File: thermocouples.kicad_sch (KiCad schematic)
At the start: 21 parts, among them J1 Conn_02x15_Odd_Even, J2 Conn_02x15_Odd_Even, J3 Conn_01x02, J4 Conn_01x02, U1 ADS1120-RVA

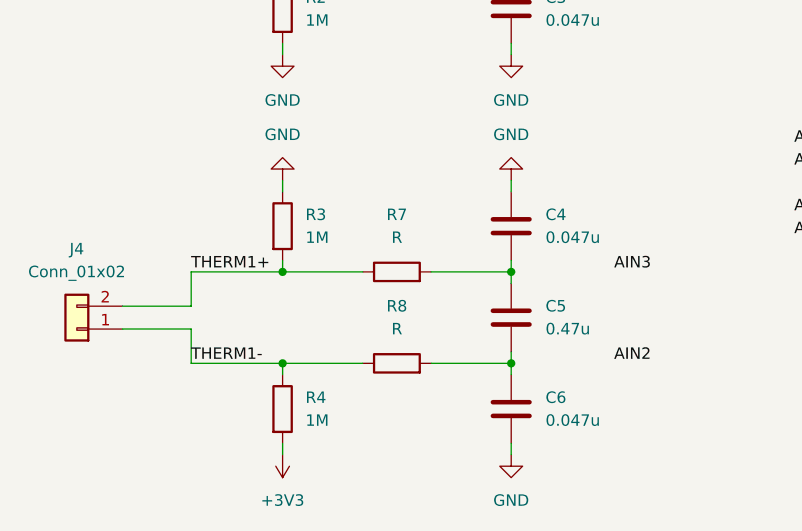
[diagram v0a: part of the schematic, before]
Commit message: sourced all components on lcsc, added ibom and outputs
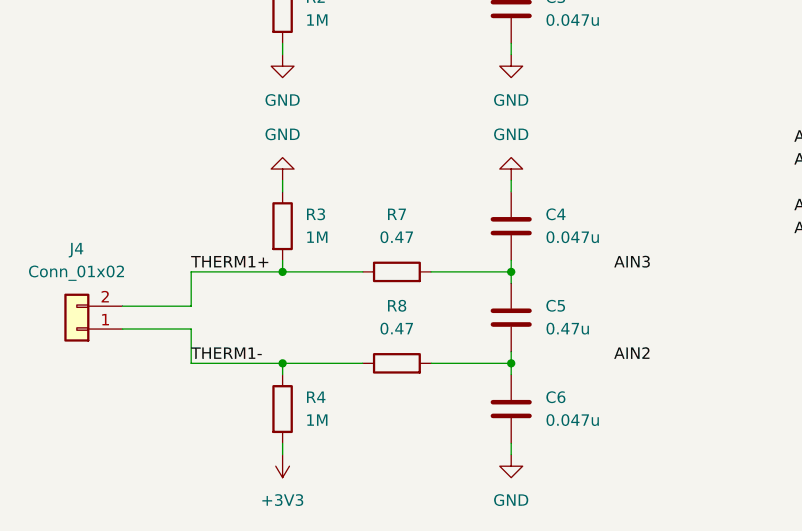
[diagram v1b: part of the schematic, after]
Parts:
- C1, C3, C4, C6: LCSC (none) -> C1622
- C2, C5: LCSC (none) -> C1623
- C7, C8: LCSC (none) -> C1591
- J1, J2, J3, J4: LCSC (none) -> C429959
- R1, R2, R3, R4: LCSC (none) -> C26098
- R5, R6: LCSC (none) -> C23411
- R7, R8: value R -> 0.47; LCSC (none) -> C23411
- U1: LCSC (none) -> C2861236
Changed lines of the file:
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@@
+      (effects (font (size 1.27 1.27)) hide)
+    )
+    (property "LCSC" "C1622" (id 4) (at 69.85 93.98 0)
       (effects (font (size 1.27 1.27)) hide)
     )
@@
     )
     (property "Datasheet" "~" (id 3) (at 247.65 107.315 0)
+      (effects (font (size 1.27 1.27)) hide)
+    )
+    (property "LCSC" "C429959" (id 4) (at 247.65 107.315 0)
       (effects (font (size 1.27 1.27)) hide)
     )
@@
       (effects (font (size 1.27 1.27)) hide)
     )
+    (property "LCSC" "C2861236" (id 4) (at 123.19 114.3 0)
+      (effects (font (size 1.27 1.27)) hide)
+    )
     (pin "1")
     (pin "10")
@@
       (effects (font (size 1.27 1.27)) hide)
     )
+    (property "LCSC" "C26098" (id 4) (at 44.45 73.66 0)
+      (effects (font (size 1.27 1.27)) hide)
+    )
     (pin "1")
     (pin "2")
@@
     )
     (property "Datasheet" "~" (id 3) (at 69.85 128.27 0)
+      (effects (font (size 1.27 1.27)) hide)
+    )
+    (property "LCSC" "C1623" (id 4) (at 69.85 128.27 0)
       (effects (font (size 1.27 1.27)) hide)
     )
@@
     )
     (property "Datasheet" "~" (id 3) (at 247.65 55.88 0)
+      (effects (font (size 1.27 1.27)) hide)
+    )
+    (property "LCSC" "C429959" (id 4) (at 247.65 55.88 0)
       (effects (font (size 1.27 1.27)) hide)
     )
@@
     (in_bom yes) (on_board yes) (fields_autoplaced)
     (property "Reference" "R8" (id 0) (at 57.15 127 90))
-    (property "Value" "R" (id 1) (at 57.15 129.54 90))
+    (property "Value" "0.47" (id 1) (at 57.15 129.54 90))
     (property "Footprint" "Resistor_SMD:R_0603_1608Metric_Pad0.98x0.95mm_HandSolder" (id 2) (at 57.15 135.128 90)
       (effects (font (size 1.27 1.27)) hide)
     )
     (property "Datasheet" "~" (id 3) (at 57.15 133.35 0)
+      (effects (font (size 1.27 1.27)) hide)
+    )
+    (property "LCSC" "C23411" (id 4) (at 57.15 133.35 0)
       (effects (font (size 1.27 1.27)) hide)
     )
@@
       (effects (font (size 1.27 1.27)) hide)
     )
+    (property "LCSC" "C429959" (id 4) (at 21.59 85.09 0)
+      (effects (font (size 1.27 1.27)) hide)
+    )
     (pin "1")
     (pin "2")
@@
       (effects (font (size 1.27 1.27)) hide)
     )
+    (property "LCSC" "C1622" (id 4) (at 69.85 73.66 0)
+      (effects (font (size 1.27 1.27)) hide)
+    )
     (pin "1")
     (pin "2")
@@
     )
     (property "Datasheet" "~" (id 3) (at 132.08 92.71 0)
+      (effects (font (size 1.27 1.27)) hide)
+    )
+    (property "LCSC" "C1591" (id 4) (at 132.08 92.71 0)
       (effects (font (size 1.27 1.27)) hide)
     )
@@
       (effects (font (size 1.27 1.27)) hide)
     )
+    (property "LCSC" "C429959" (id 4) (at 21.59 129.54 0)
+      (effects (font (size 1.27 1.27)) hide)
+    )
     (pin "1")
     (pin "2")
@@
       (effects (font (size 1.27 1.27)) hide)
     )
+    (property "LCSC" "C26098" (id 4) (at 44.45 118.11 0)
+      (effects (font (size 1.27 1.27)) hide)
+    )
     (pin "1")
     (pin "2")
@@
     )
     (property "Datasheet" "~" (id 3) (at 69.85 118.11 0)
+      (effects (font (size 1.27 1.27)) hide)
+    )
+    (property "LCSC" "C1622" (id 4) (at 69.85 118.11 0)
       (effects (font (size 1.27 1.27)) hide)
     )
@@
       (effects (font (size 1.27 1.27)) hide)
     )
+    (property "LCSC" "C23411" (id 4) (at 57.15 78.74 0)
+      (effects (font (size 1.27 1.27)) hide)
+    )
     (pin "1")
     (pin "2")
@@
       (effects (font (size 1.27 1.27)) hide)
     )
+    (property "LCSC" "C26098" (id 4) (at 44.45 138.43 0)
+      (effects (font (size 1.27 1.27)) hide)
+    )
     (pin "1")
     (pin "2")
@@
       (effects (font (size 1.27 1.27)) hide)
     )
+    (property "LCSC" "C1623" (id 4) (at 69.85 83.82 0)
+      (effects (font (size 1.27 1.27)) hide)
+    )
     (pin "1")
     (pin "2")
@@
     )
     (property "Datasheet" "~" (id 3) (at 115.57 92.71 0)
+      (effects (font (size 1.27 1.27)) hide)
+    )
+    (property "LCSC" "C1591" (id 4) (at 115.57 92.71 0)
       (effects (font (size 1.27 1.27)) hide)
     )
@@
     (in_bom yes) (on_board yes) (fields_autoplaced)
     (property "Reference" "R7" (id 0) (at 57.15 116.84 90))
-    (property "Value" "R" (id 1) (at 57.15 119.38 90))
+    (property "Value" "0.47" (id 1) (at 57.15 119.38 90))
     (property "Footprint" "Resistor_SMD:R_0603_1608Metric_Pad0.98x0.95mm_HandSolder" (id 2) (at 57.15 124.968 90)
       (effects (font (size 1.27 1.27)) hide)
     )
     (property "Datasheet" "~" (id 3) (at 57.15 123.19 0)
+      (effects (font (size 1.27 1.27)) hide)
+    )
+    (property "LCSC" "C23411" (id 4) (at 57.15 123.19 0)
       (effects (font (size 1.27 1.27)) hide)
     )
@@
     )
     (property "Datasheet" "~" (id 3) (at 69.85 138.43 0)
+      (effects (font (size 1.27 1.27)) hide)
+    )
+    (property "LCSC" "C1622" (id 4) (at 69.85 138.43 0)
       (effects (font (size 1.27 1.27)) hide)
     )
@@
       (effects (font (size 1.27 1.27)) hide)
     )
+    (property "LCSC" "C23411" (id 4) (at 57.15 88.9 0)
+      (effects (font (size 1.27 1.27)) hide)
+    )
     (pin "1")
     (pin "2")
@@
     )
     (property "Datasheet" "~" (id 3) (at 44.45 93.98 0)
+      (effects (font (size 1.27 1.27)) hide)
+    )
+    (property "LCSC" "C26098" (id 4) (at 44.45 93.98 0)
       (effects (font (size 1.27 1.27)) hide)
     )
@@
     )
     (path "/d0ba2805-cdc7-4783-a4c1-128cd33a8d11"
-      (reference "R7") (unit 1) (value "R") (footprint "Resistor_SMD:R_0603_1608Metric_Pad0.98x0.95mm_HandSolder")
+      (reference "R7") (unit 1) (value "0.47") (footprint "Resistor_SMD:R_0603_1608Metric_Pad0.98x0.95mm_HandSolder")
     )
     (path "/2af28dc9-d4c7-4a74-8fce-775395b63c96"
-      (reference "R8") (unit 1) (value "R") (footprint "Resistor_SMD:R_0603_1608Metric_Pad0.98x0.95mm_HandSolder")
+      (reference "R8") (unit 1) (value "0.47") (footprint "Resistor_SMD:R_0603_1608Metric_Pad0.98x0.95mm_HandSolder")
     )
     (path "/1a7c0ad3-6f69-49b6-82da-43d1874349bb"
